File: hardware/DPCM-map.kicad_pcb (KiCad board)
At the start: 2 copper layers, 178 x 178 mm, 106 parts, among them J1 JMP, J10 Conn_01x03_Female, J2 Conn_01x06_Male, J3 Touch_Pad_+, J4 Touch_Pad_0, J5 Touch_Pad_-, J6 JMP, J7 Conn_01x06_Female, J8 Conn_01x03_Female, J9 Conn_01x03_Female, P1 USB_C_Plug, Q1 2N7002, Q2 2N7002, SW1 SW_Push, SW2 SW_+_Fb, SW3 SW_0_Fb, SW4 SW_-_Fb, U1 AZ1117-3.3, U2 BME280, U4 ESP32-WROOM-32, U5 CH340G, Y1 12MHz

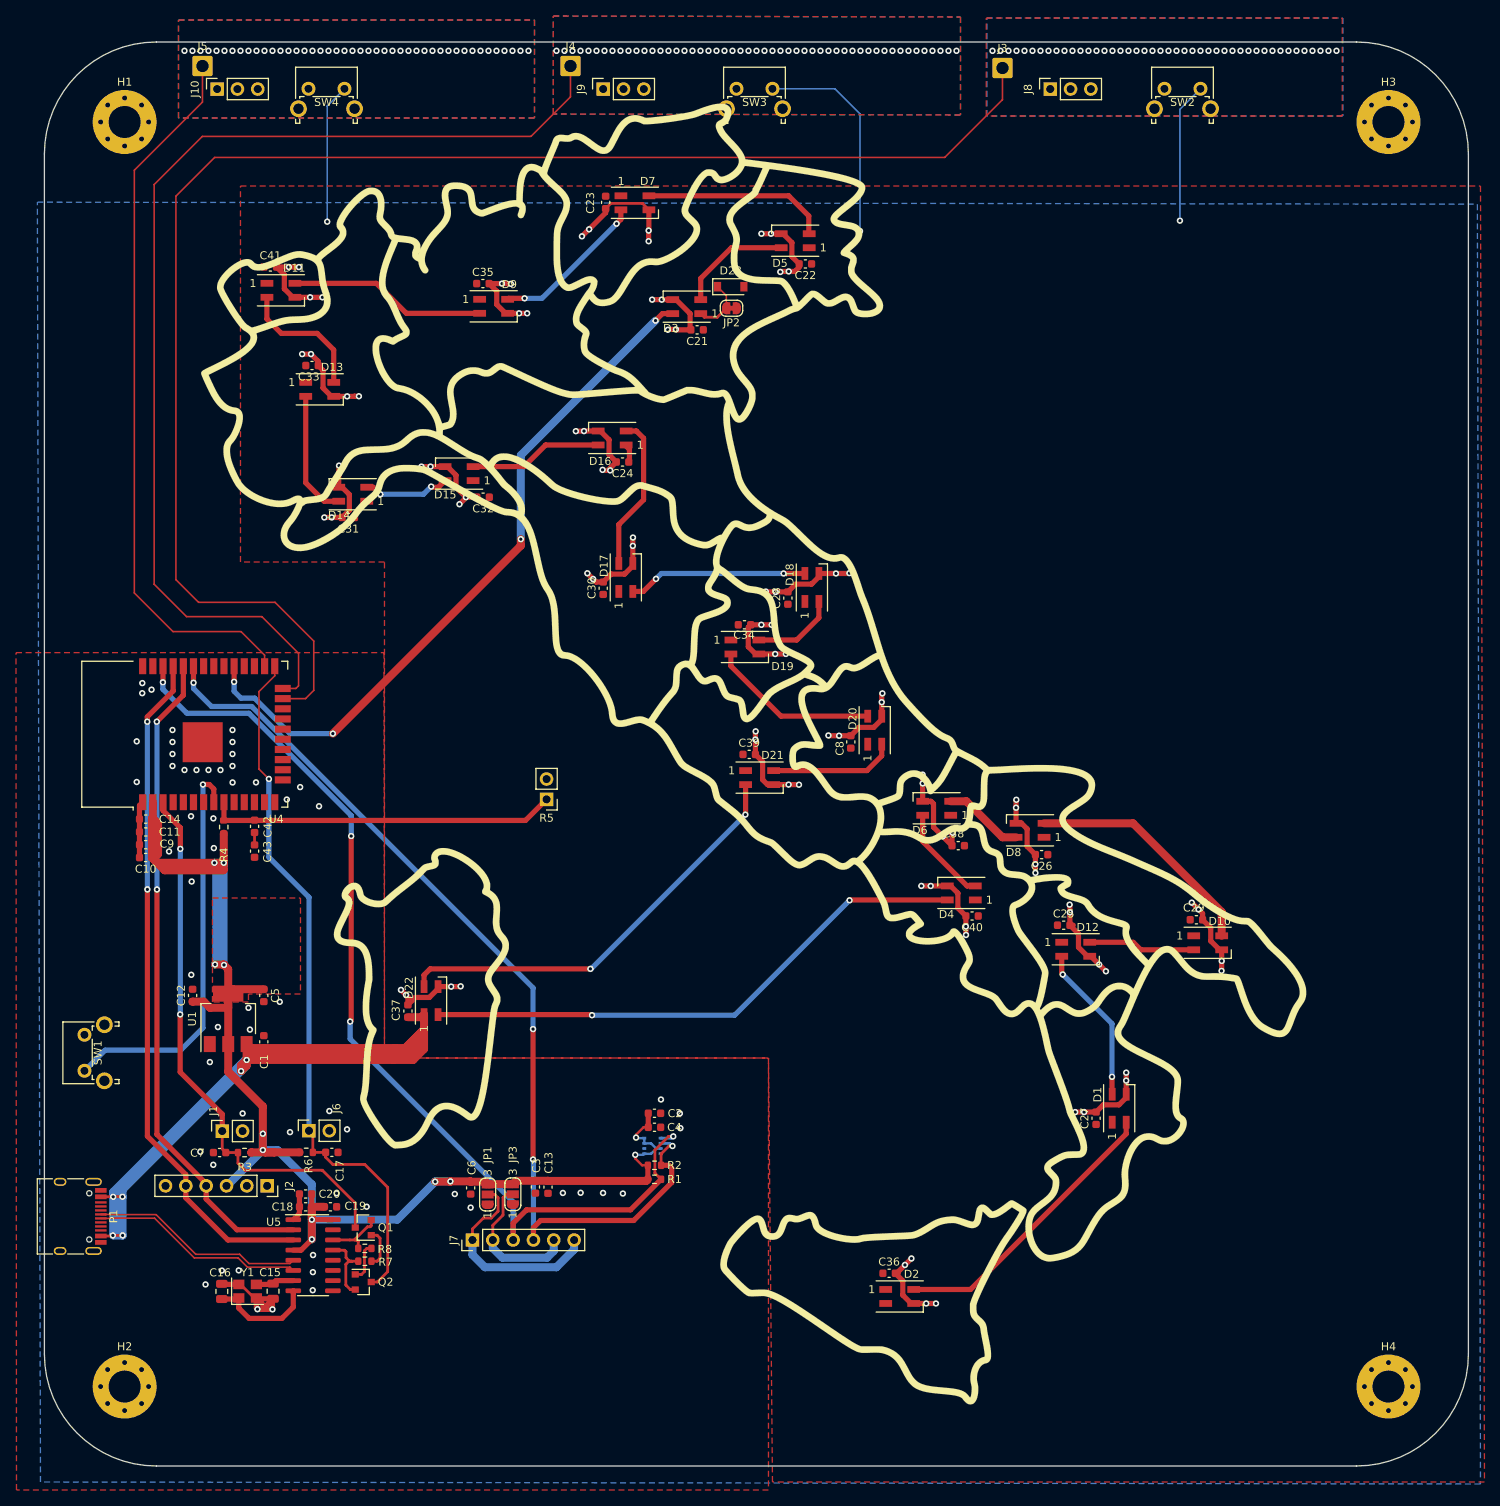
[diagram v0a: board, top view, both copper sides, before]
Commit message: change new ws footprints
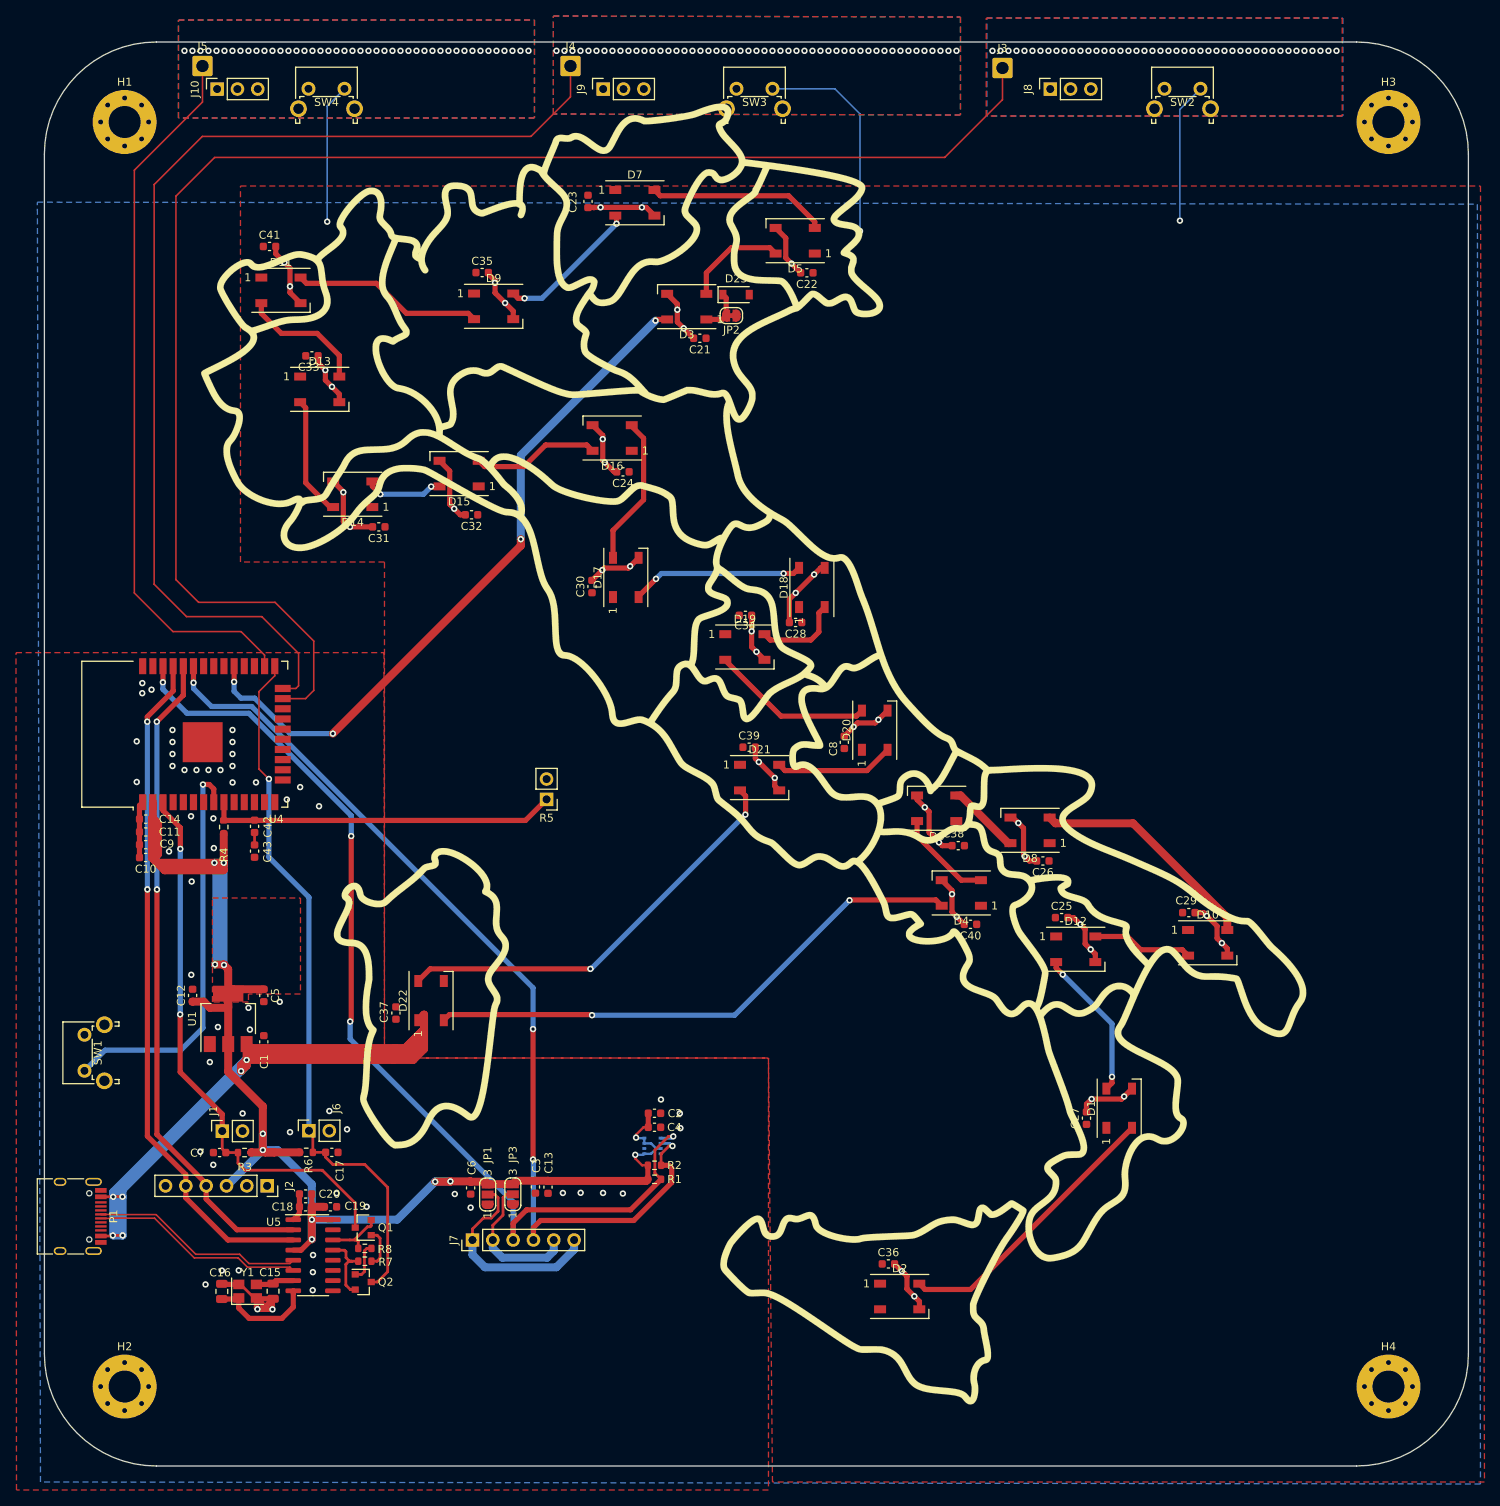
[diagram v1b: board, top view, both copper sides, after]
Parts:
- D1, D10, D11, D12, D13, D14, D15, D16, D17, D18, D19, D2, D20, D21, D22, D3, D4, D5, D6, D7, D8, D9: footprint LED_SMD:LED_SK6812MINI_PLCC4_3.5x3.5mm_P1.75mm -> LED_SMD:LED_WS2812B_PLCC4_5.0x5.0mm_P3.2mm
- moved C31 3.99 mm to (152.3, 110.6)
- moved C28 3.20 mm to (204.4, 122.6), turned to 180 degrees
- moved C32 2.63 mm to (163.9, 109.1)
- moved C41 2.57 mm to (138.6, 75.6)
- moved C23 2.21 mm to (178.4, 69.9)
- moved C37 1.52 mm to (154.4, 171.4)
- moved C30 1.42 mm to (178.9, 118.1)
- moved C35 1.38 mm to (165.2, 78.8)
- moved C29 1.30 mm to (253.5, 158.8)
- moved C24 1.23 mm to (182.8, 103.7)
- moved C33 1.21 mm to (143.9, 89.2)
- moved C27 1.20 mm to (240.8, 184.5)
- moved D23 1.20 mm to (196.9, 81.6)
- moved C34 1.19 mm to (198.1, 121.7)
- moved C36 1.17 mm to (216.0, 202.7)
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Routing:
- net GND: track 334.5 -> 251.8 mm, vias 149 -> 101
- net +5V: track 164.0 -> 160.0 mm
- net Net-(D23-Pad1): track 7.00 -> 5.47 mm
- net Net-(D3-Pad2): track 14.3 -> 12.9 mm
- net Net-(D7-Pad2): track 19.5 -> 18.1 mm
- net Net-(D14-Pad2): track 10.9 -> 9.89 mm
- net LED_CHAIN: track 88.5 -> 87.5 mm
- net Net-(D19-Pad2): track 21.2 -> 20.4 mm
- net Net-(D11-Pad2): track 16.7 -> 15.9 mm
- net Net-(D21-Pad2): track 53.7 -> 52.9 mm
- net Net-(D13-Pad2): track 15.9 -> 15.0 mm
- net Net-(D22-Pad2): track 69.7 -> 68.8 mm
- net Net-(D10-Pad4): track 29.8 -> 28.9 mm
- net Net-(D1-Pad4): track 19.9 -> 19.0 mm
- net Net-(D17-Pad2): track 22.4 -> 21.6 mm
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
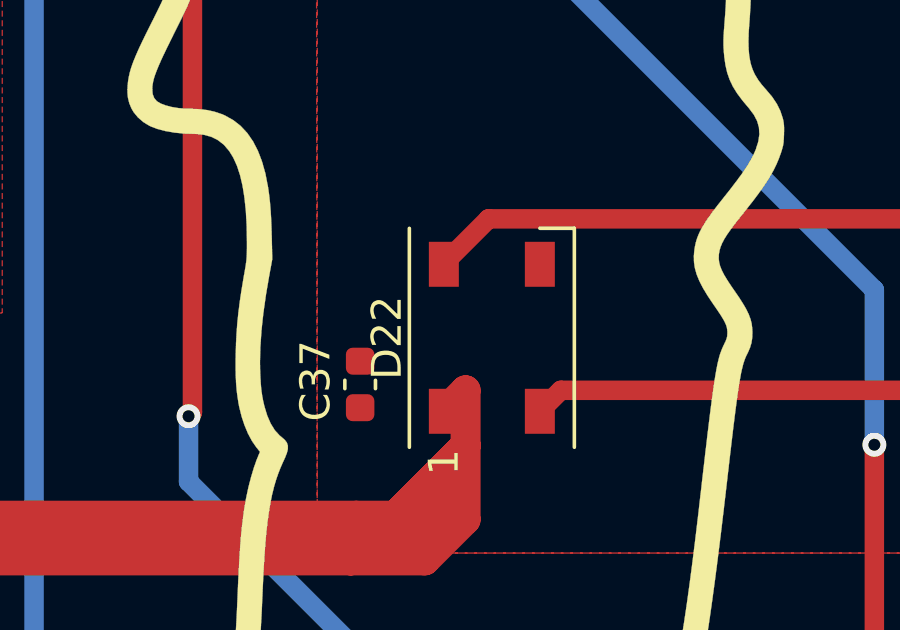
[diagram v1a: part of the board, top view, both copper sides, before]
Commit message: added missing led ground
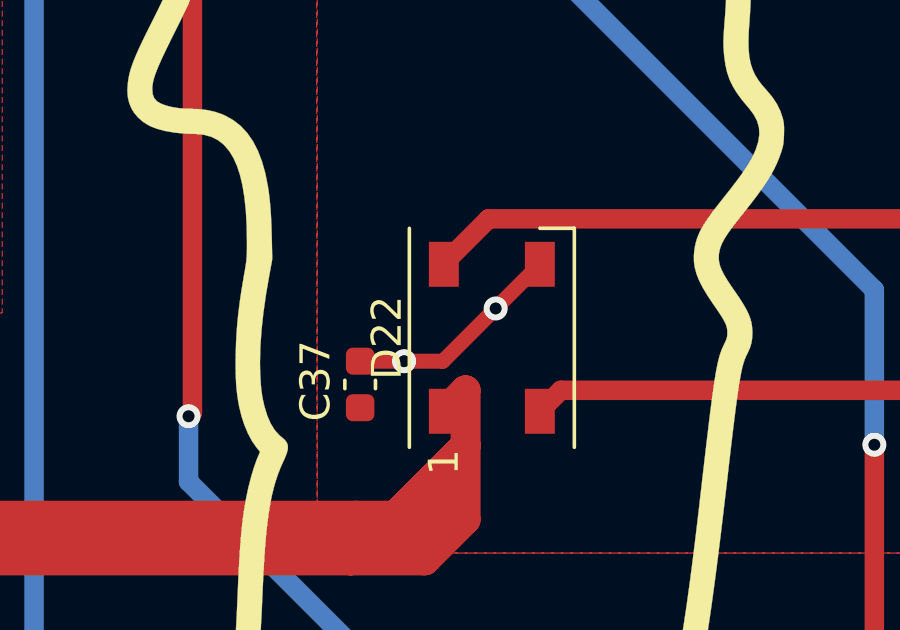
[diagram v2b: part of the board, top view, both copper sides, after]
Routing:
- net GND: track 251.8 -> 259.2 mm, vias 101 -> 103

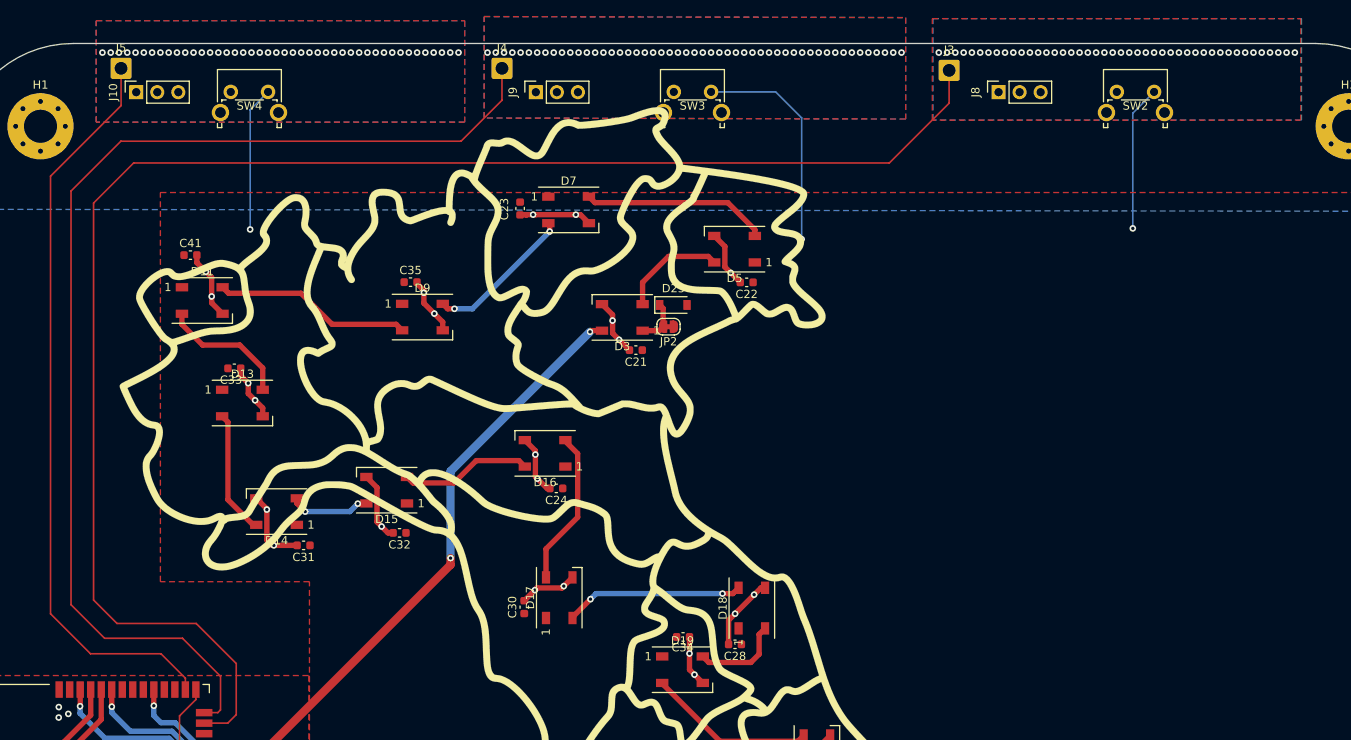
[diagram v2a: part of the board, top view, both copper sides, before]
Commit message: increased spacing between touch pads as per st appnote
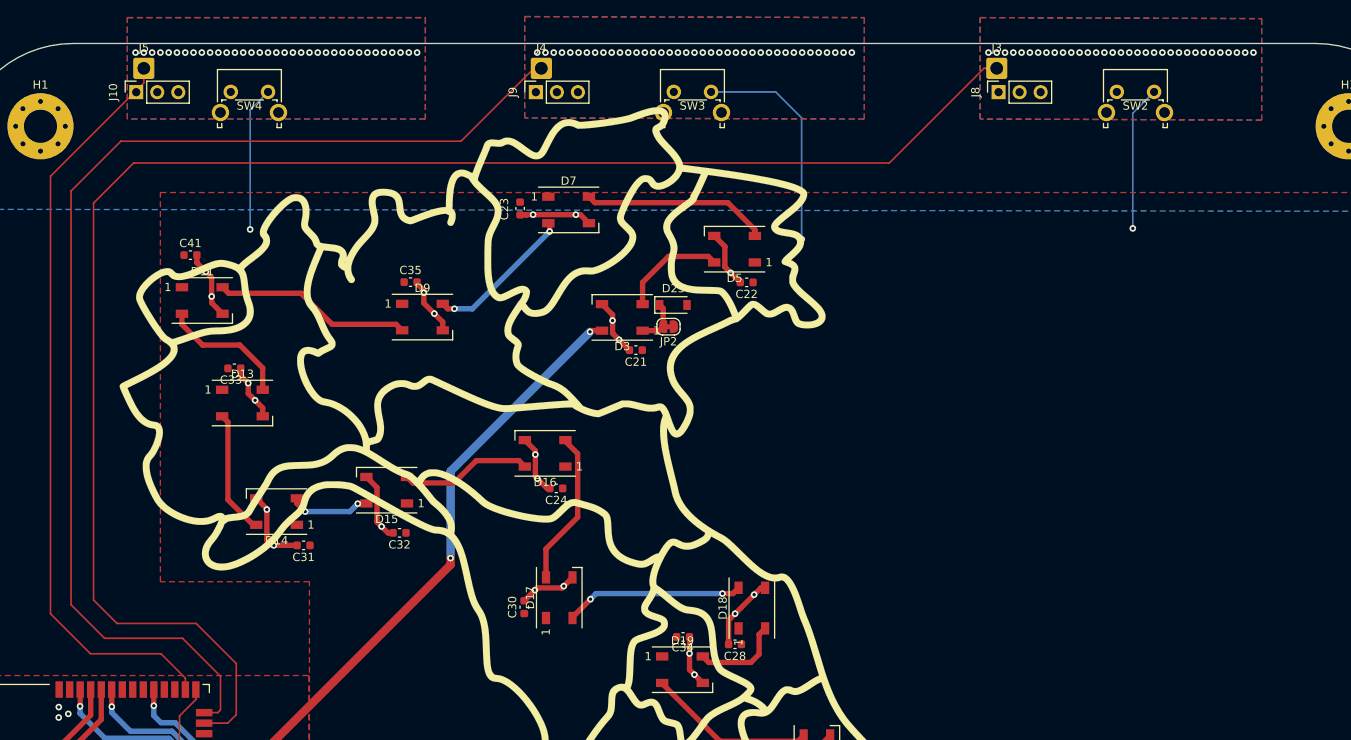
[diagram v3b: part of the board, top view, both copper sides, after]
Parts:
- moved J3 5.76 mm to (236.0, 53.0)
- moved J4 4.75 mm to (181.0, 53.0)
- moved J5 2.75 mm to (133.0, 53.0)
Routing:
- net TOUCH_+: track 191.1 -> 194.6 mm, vias 44 -> 33
- net TOUCH_0: track 138.2 -> 140.7 mm, vias 51 -> 39
- net TOUCH_-: track 90.3 -> 91.4 mm, vias 44 -> 35
